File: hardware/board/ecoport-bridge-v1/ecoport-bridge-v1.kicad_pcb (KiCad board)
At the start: 2 copper layers, 51.5 x 92 mm, 71 parts, among them J1 420B2V12FL0, J2 Conn_01x02, J3 SM04B-SRSS-TB, J4 USB4085-GF-A, J5 Conn_01x02, J6 Connector Wire, J7 B3B-PH-K-S, SW1 RESET, SW2 BOOT, U1 IRM-05-5, U2 TLV75733PDBVR, U3 SP3485EET, U4 USBLC6-2SC6, U5 SN74LV1T34DCKR, U6 ESP32-C6-WROOM-1-N8, U7 USBLC6-2SC6, U8 LM66100DCKR

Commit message: Pull J1 pin 9, fill in MPNs, 1A fuse, rev-a release assets
- Remove J1 pin 9 (NC) from symbol, footprint and board: its floating pad
  sat 4.4 mm from F1 and 1.6 mm from pin 8, short of 5.5 mm creepage.
  Pull list is now pins 4, 6, 9, 10, 11.
- F1 to SF-2410SP100W-2 (1 A time-lag) for inrush margin; footprint fields
  and assembly notes updated to match.
- J3 is the top-entry BM04B-SRSS-TB to match its footprint.
- Add missing MPN/Manufacturer for U6, J7, J3, D2/D3 (value typo SKC6812 ->
  SK6812) and TP14, and include TP14 in the BOM.
- hardware/rev-a: populated bom.csv, DigiKey upload file for 6 boards,
  interactive BOM, board STEP for the enclosure (3d/), images/ for visual
  assets, and a README describing the folder.
- .gitignore: STEP and bom/ exports next to the KiCad project.

Co-Authored-By: Claude Opus 5.5 <noreply@anthropic.com>
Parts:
- added kobee-studio-6AD3D2C7: Kobee Studio, kobee-studio-6AD3D2C7, F.Cu at (97.1, 87.5)
- added kobee-studio-6AD3E735: Kobee Studio, kobee-studio-6AD3E735, F.Cu at (97.3, 69.2)
- D2, D3: value SKC6812 -> SK6812
- F1: value SF-2410SP050W-2 -> SF-2410SP100W-2
- J3: value SM04B-SRSS-TB -> BM04B-SRSS-TB
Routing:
- net /EN: track 70.0 -> 70.7 mm
- net GND: vias 123 -> 125
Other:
- board text added: "Vendor"

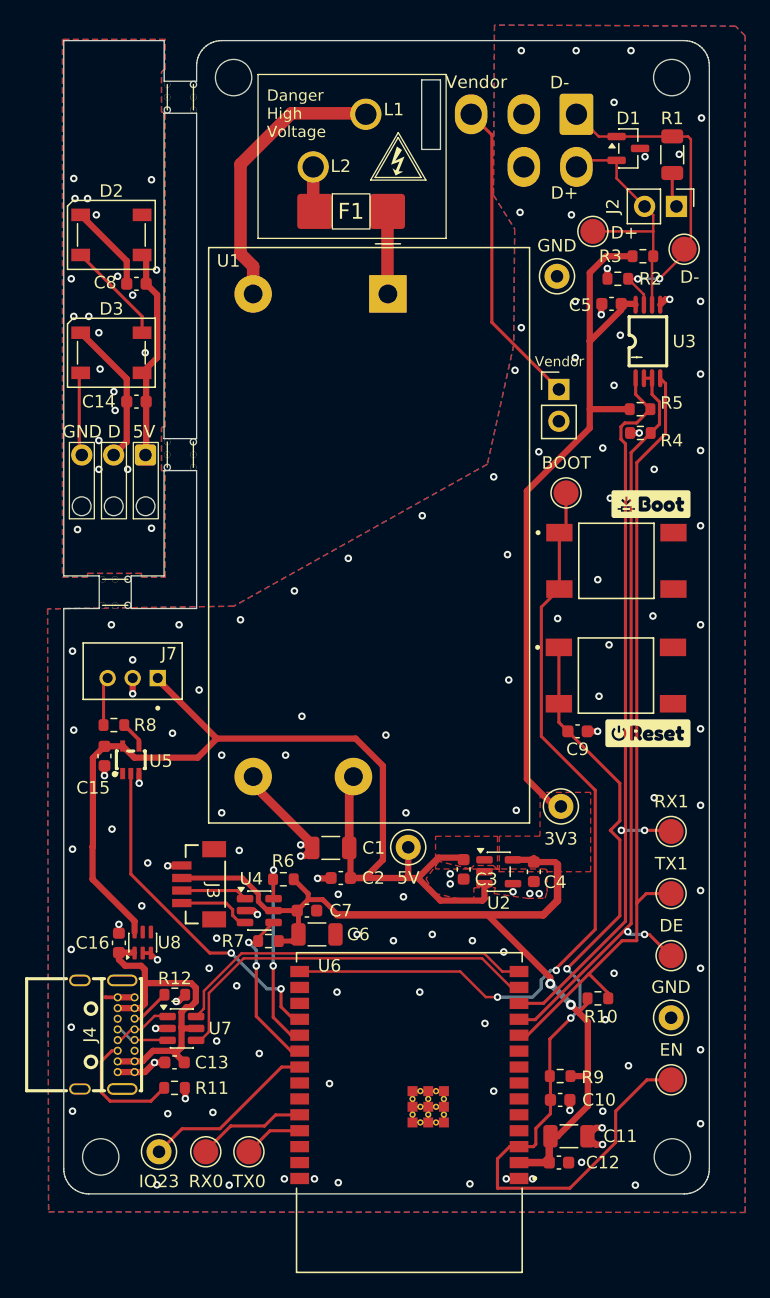
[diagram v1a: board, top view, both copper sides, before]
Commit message: Rework board outline and mouse-bite tabs; ignore reference PDFs
- New outline and LED-strip tab positions; lower tab sized to fit the
  3-hole mouse bites.
- docs/*.pdf ignored: copyrighted CTA-2045 / EPRI references stay local.

Co-Authored-By: Claude Opus 5.5 <noreply@anthropic.com>
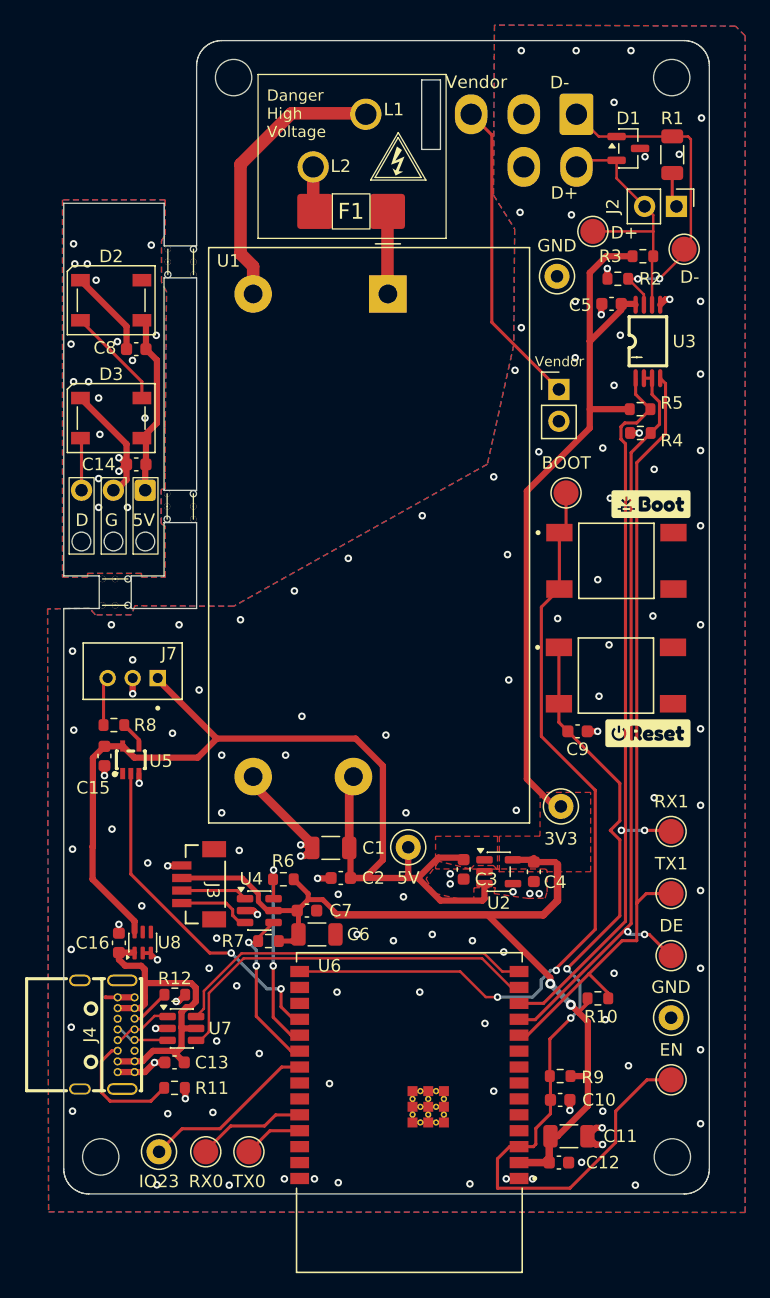
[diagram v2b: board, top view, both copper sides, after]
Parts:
- moved REF** 13.1 mm to (58.5, 49.9)
- moved REF** 13.1 mm to (61.1, 49.9)
- moved C8 5.21 mm to (56.3, 56.8)
- moved D2 5.21 mm to (54.3, 52.9)
- moved D3 5.21 mm to (54.3, 62.3)
- moved C14 5.01 mm to (56.3, 66.0)
- moved REF** 4.13 mm to (58.5, 69.4)
- moved REF** 4.13 mm to (61.1, 69.4)
- moved J6 2.81 mm to (51.9, 68.1)
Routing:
- net LED_5V: track 17.1 -> 14.7 mm
- net /LED_DIN: track 6.68 -> 4.63 mm
- net LED_GND: track 18.7 -> 18.1 mm, vias 21 -> 19
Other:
- outline, holes or cut-outs redrawn
- board text added: "G"
- board text removed: "GND"
